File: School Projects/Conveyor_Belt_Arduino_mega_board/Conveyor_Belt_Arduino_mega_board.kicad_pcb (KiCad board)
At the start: 2 copper layers, 94.5 x 90.8 mm, 23 parts, among them J1 Conn_01x08_Pin, J2 Conn_01x08_Pin, J3 Conn_01x08_Pin, J4 Conn_01x08_Pin, J5 Conn_01x08_Pin, J6 Conn_01x10_Pin

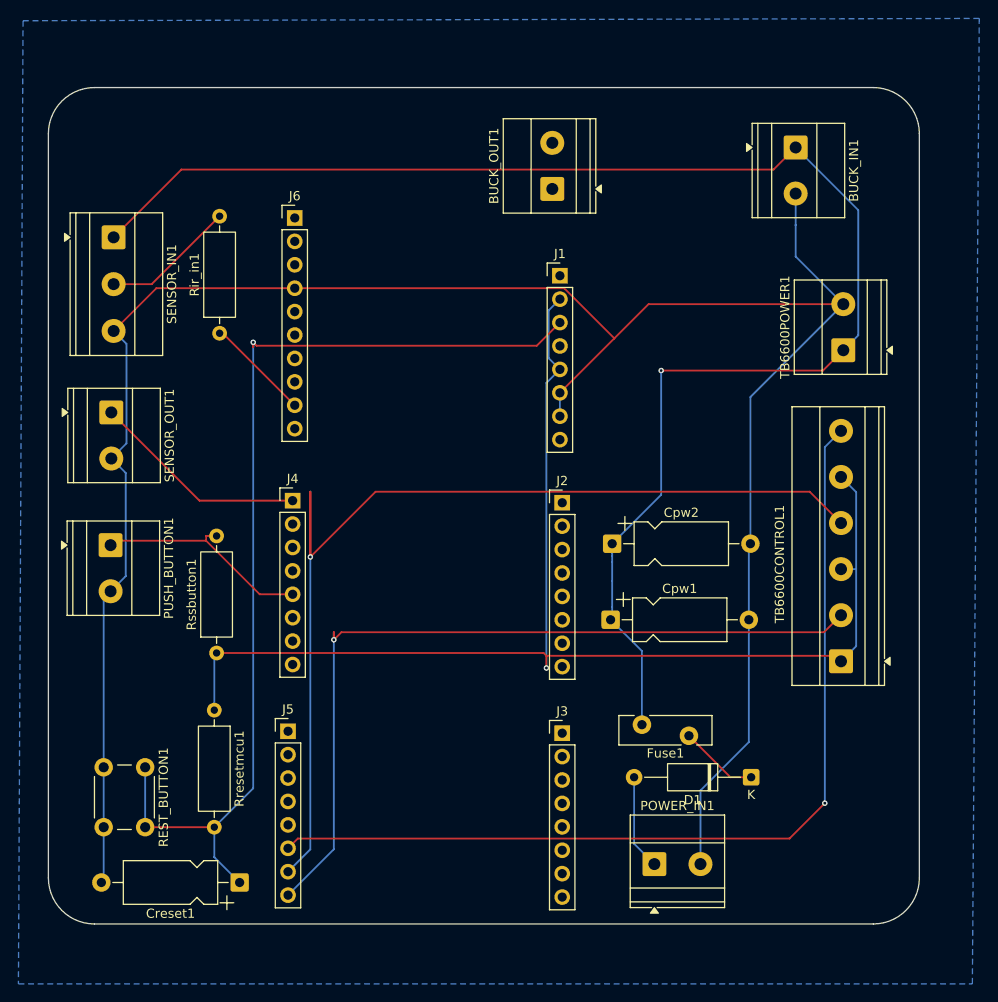
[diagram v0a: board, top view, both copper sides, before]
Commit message: Removed some unnecessary parts like reset button and emergency stop based on final production board
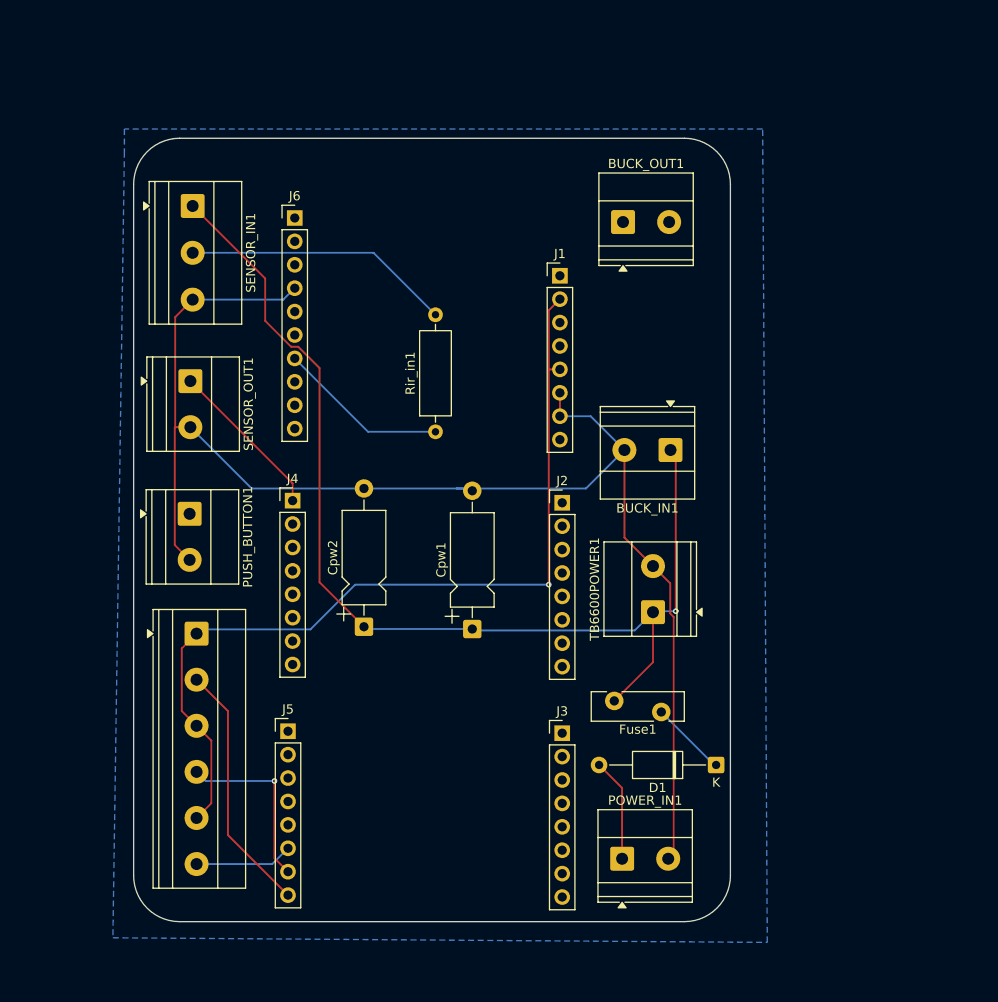
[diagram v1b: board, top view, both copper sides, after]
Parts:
- removed Creset1: 0.1uF, Capacitor_THT:CP_Axial_L10.0mm_D4.5mm_P15.00mm_Horizontal
- removed REST_BUTTON1: RST_BTN, Button_Switch_THT:SW_PUSH_6mm
- removed Rresetmcu1, Rssbutton1: 10KΩ, Resistor_THT:R_Axial_DIN0309_L9.0mm_D3.2mm_P12.70mm_Horizontal
- moved TB6600CONTROL1 70.0 mm to (113.8, 119.0), turned to -90 degrees
- moved BUCK_IN1 35.5 mm to (165.2, 99.1), turned to 180 degrees
- moved TB6600POWER1 35.1 mm to (163.3, 116.7)
- moved Cpw2 28.4 mm to (132.0, 118.2), turned to 90 degrees
- moved Rir_in1 25.7 mm to (139.8, 97.1)
- moved Cpw1 15.0 mm to (143.7, 118.5), turned to 90 degrees
- moved PUSH_BUTTON1 9.23 mm to (113.1, 106.0)
- moved SENSOR_IN1 9.23 mm to (113.4, 72.6)
- moved SENSOR_OUT1 9.23 mm to (113.2, 91.6)
- moved BUCK_OUT1 8.48 mm to (160.1, 74.3), turned to 0 degrees
- moved D1 4.03 mm to (170.2, 133.2)
- moved Fuse1 3.96 mm to (164.2, 127.5)
- moved POWER_IN1 3.55 mm to (160.0, 143.4)
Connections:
- J1 pad 3: /Reset -> unconnected-(J1-Pin_3-Pad3)
- J4 pad 5: /S/S button -> unconnected-(J4-Pin_5-Pad5)
- J6 pad 7: unconnected-(J6-Pin_7-Pad7) -> /IR_IN
- J6 pad 9: /IR_IN -> unconnected-(J6-Pin_9-Pad9)
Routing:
- net /Reset: track 112.0 -> 0.00 mm, vias 1 -> 0
- net /DIR: track 125.4 -> 19.3 mm
- net /EN: track 101.4 -> 10.6 mm, vias 1 -> 0
- net GND: track 239.9 -> 154.2 mm
- net /PUL: track 89.2 -> 27.5 mm, vias 1 -> 0
- net /24V: track 166.3 -> 118.7 mm
- net /5V: track 140.4 -> 95.8 mm
- net /S/S button: track 24.0 -> 0.00 mm
- net Net-(SENSOR_IN1-Pin_2): track 14.6 -> 29.1 mm
- net /IR_IN: track 11.4 -> 18.6 mm
- net /IR_OUT: track 23.6 -> 17.6 mm
- net Net-(D1-A): track 10.3 -> 11.2 mm
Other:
- board size 94.5 x 90.8 mm -> 64.8 x 85 mm
